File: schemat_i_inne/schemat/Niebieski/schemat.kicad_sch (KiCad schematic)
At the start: 30 parts, among them J1 Hole1, J2 Hole2, J3 Hole3, J4 Hole4, J5 RJ45, SW1 SW_DIP_x01, SW2 Left, SW3 Up, SW4 Down, SW5 Right, SW6 Jump, SW7 Punch, U1 ATmega32A-AU, U2 L7805, U3 WG12864B-STBL, U4 LF33_TO252, U5 SN74LS07, U6 SD, Y1 16Mhz

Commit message: Good footprints, before changes on PCB
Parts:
- U5: footprint Package_TO_SOT_SMD:TO-252-2 -> Package_DIP:DIP-14_W7.62mm_LongPads
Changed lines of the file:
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@@
     (property "Reference" "U5" (id 0) (at 166.37 54.7202 0))
     (property "Value" "SN74LS07" (id 1) (at 166.37 57.2571 0))
-    (property "Footprint" "Package_TO_SOT_SMD:TO-252-2" (id 2) (at 166.37 62.23 0)
+    (property "Footprint" "Package_DIP:DIP-14_W7.62mm_LongPads" (id 2) (at 166.37 62.23 0)
       (effects (font (size 1.27 1.27)) hide)
     )
@@
       (effects (font (size 1.27 1.27)) (justify left))
     )
-    (property "Footprint" "Package_TO_SOT_SMD:TO-252-2" (id 2) (at 226.06 30.48 0)
+    (property "Footprint" "Package_DIP:DIP-14_W7.62mm_LongPads" (id 2) (at 226.06 30.48 0)
       (effects (font (size 1.27 1.27)) hide)
     )
@@
     (property "Reference" "U5" (id 0) (at 165.1 67.4202 0))
     (property "Value" "SN74LS07" (id 1) (at 165.1 69.9571 0))
-    (property "Footprint" "Package_TO_SOT_SMD:TO-252-2" (id 2) (at 165.1 74.93 0)
+    (property "Footprint" "Package_DIP:DIP-14_W7.62mm_LongPads" (id 2) (at 165.1 74.93 0)
       (effects (font (size 1.27 1.27)) hide)
     )
@@
     (property "Reference" "U5" (id 0) (at 165.1 29.3202 0))
     (property "Value" "SN74LS07" (id 1) (at 165.1 31.8571 0))
-    (property "Footprint" "Package_TO_SOT_SMD:TO-252-2" (id 2) (at 165.1 36.83 0)
+    (property "Footprint" "Package_DIP:DIP-14_W7.62mm_LongPads" (id 2) (at 165.1 36.83 0)
       (effects (font (size 1.27 1.27)) hide)
     )
@@
     (property "Reference" "U5" (id 0) (at 165.1 42.0202 0))
     (property "Value" "SN74LS07" (id 1) (at 165.1 44.5571 0))
-    (property "Footprint" "Package_TO_SOT_SMD:TO-252-2" (id 2) (at 165.1 49.53 0)
+    (property "Footprint" "Package_DIP:DIP-14_W7.62mm_LongPads" (id 2) (at 165.1 49.53 0)
       (effects (font (size 1.27 1.27)) hide)
     )
@@
     )
     (path "/6cfeab45-cb3f-4496-a149-1dcab4f48b9e"
-      (reference "U5") (unit 1) (value "SN74LS07") (footprint "Package_TO_SOT_SMD:TO-252-2")
+      (reference "U5") (unit 1) (value "SN74LS07") (footprint "Package_DIP:DIP-14_W7.62mm_LongPads")
     )
     (path "/97028cc7-c78a-4d63-bf12-fed98ab2a824"
-      (reference "U5") (unit 2) (value "SN74LS07") (footprint "Package_TO_SOT_SMD:TO-252-2")
+      (reference "U5") (unit 2) (value "SN74LS07") (footprint "Package_DIP:DIP-14_W7.62mm_LongPads")
     )
     (path "/143f8ad6-39a7-42cd-8611-e300b4175f5e"
-      (reference "U5") (unit 3) (value "SN74LS07") (footprint "Package_TO_SOT_SMD:TO-252-2")
+      (reference "U5") (unit 3) (value "SN74LS07") (footprint "Package_DIP:DIP-14_W7.62mm_LongPads")
     )
     (path "/5c70e1c2-d58b-40cb-968e-ca7279c6263b"
-      (reference "U5") (unit 4) (value "SN74LS07") (footprint "Package_TO_SOT_SMD:TO-252-2")
+      (reference "U5") (unit 4) (value "SN74LS07") (footprint "Package_DIP:DIP-14_W7.62mm_LongPads")
     )
     (path "/2e4c2d57-8d82-46dc-a18a-d07a5b5f91e8"
-      (reference "U5") (unit 7) (value "SN74LS07") (footprint "Package_TO_SOT_SMD:TO-252-2")
+      (reference "U5") (unit 7) (value "SN74LS07") (footprint "Package_DIP:DIP-14_W7.62mm_LongPads")
     )
     (path "/cd6fa7d4-14f3-428e-b040-5de477b5d49d"

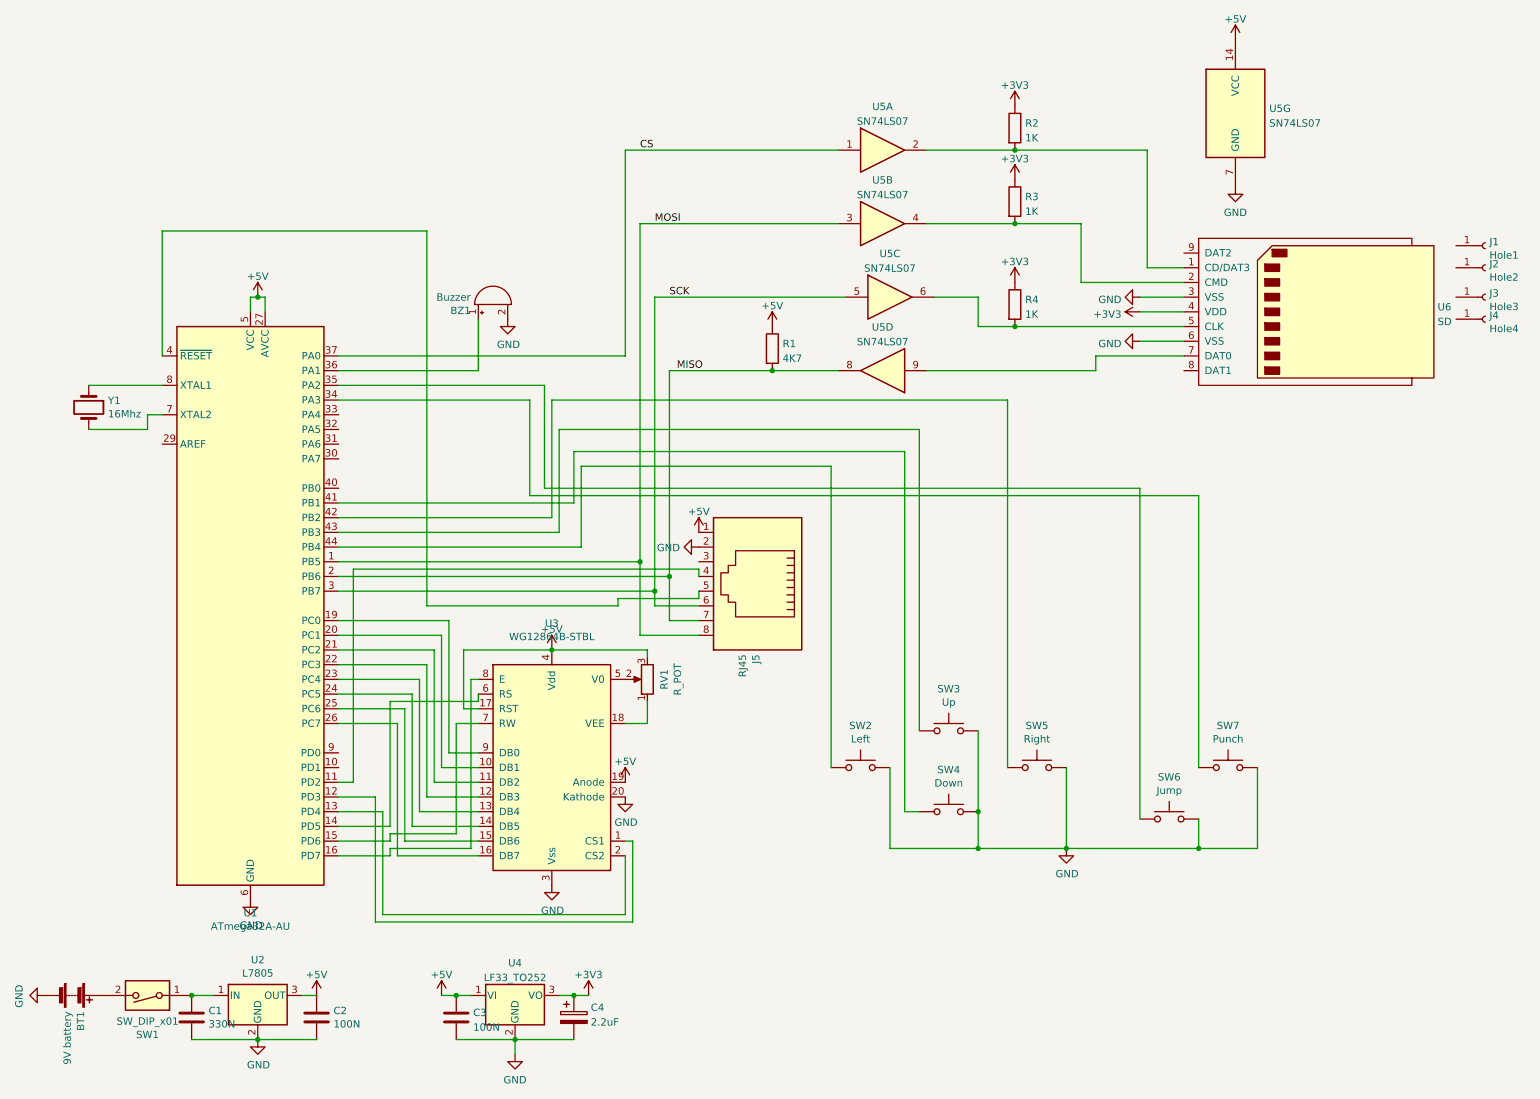
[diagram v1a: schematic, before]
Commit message: Wstepne sciezki z buforem
-> Dodano wstepne sciezki razem z buforem
-> Tam gdzie bylo to wymagane zmieniono warstwe
-> Dodano oporniki 0R we wlasciwych miejscach
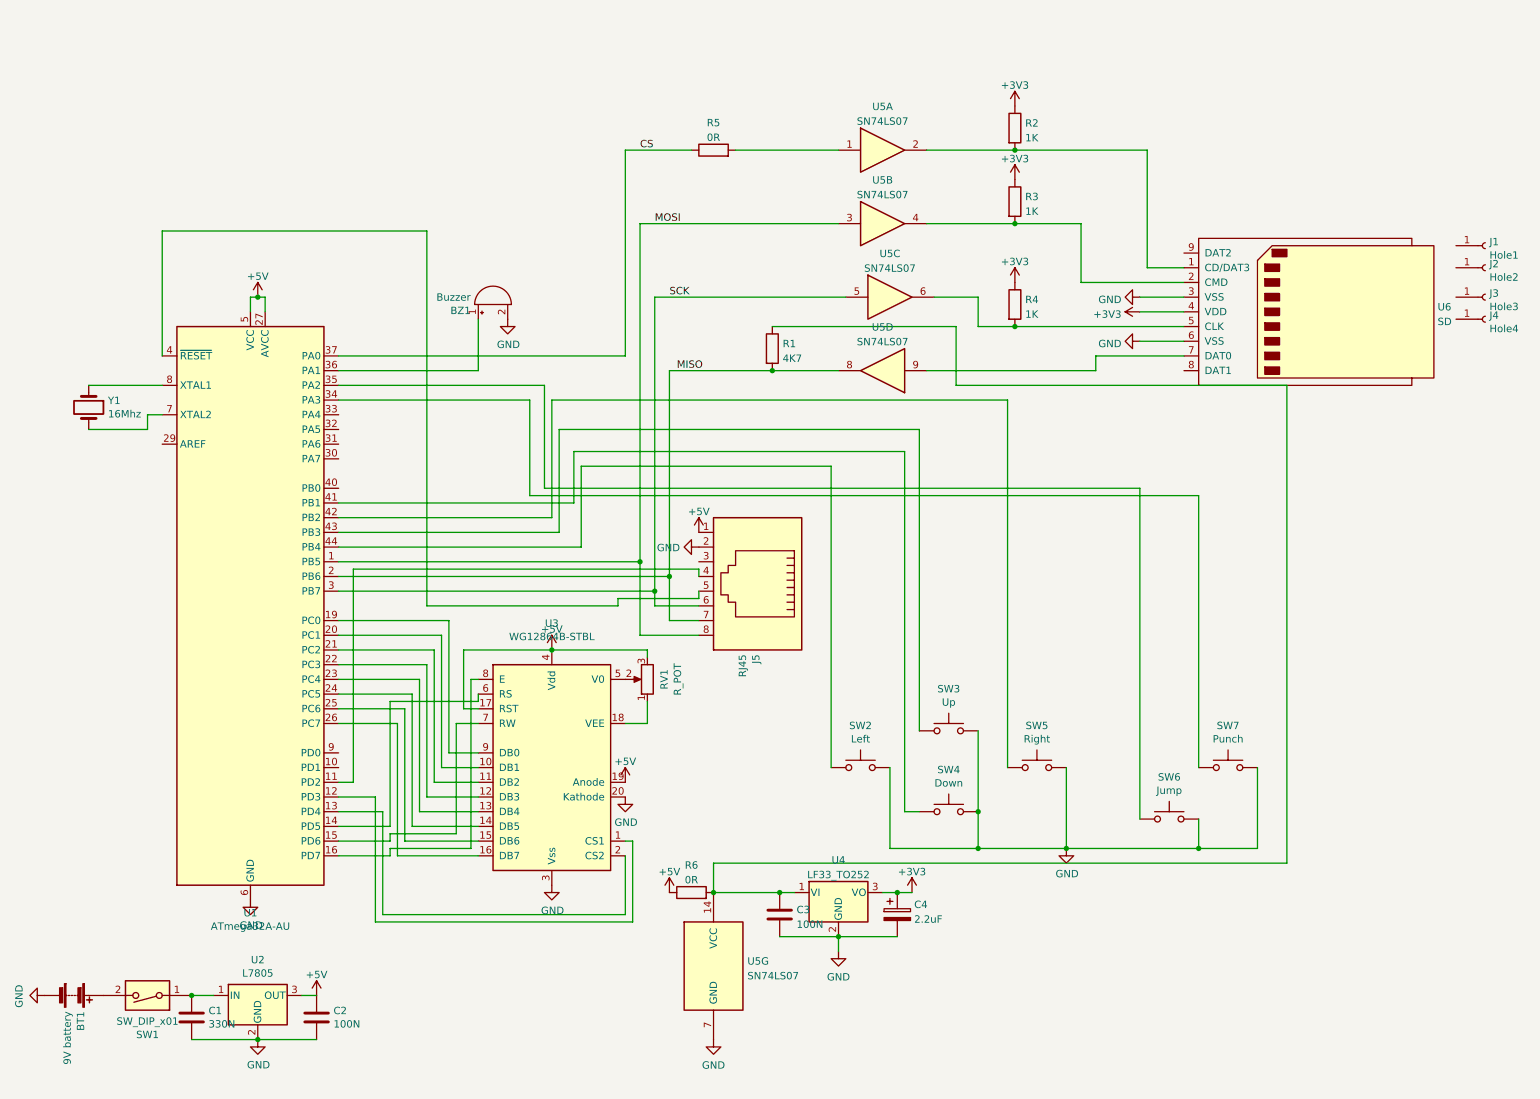
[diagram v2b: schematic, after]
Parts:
- added R5, R6: 0R, Resistor_THT:R_Axial_DIN0207_L6.3mm_D2.5mm_P10.16mm_Horizontal, symbol Device:R
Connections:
- net +5V: now also R6.1; no longer C3.1, R1.1, U4.1 (VI), U5.14 (VCC)
- net CS: now also R5.1; no longer U5.1
- new net: C3.1, R1.1, R6.2, U4.1 (VI), U5.14 (VCC)
- new net: R5.2, U5.1
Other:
- moved on the sheet: C3, C4, U4, U5G

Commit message: Awful but should work v2
-> Wszystko zostalo prowizorycznie podlaczone
-> uzyto 3 opornikow 0R
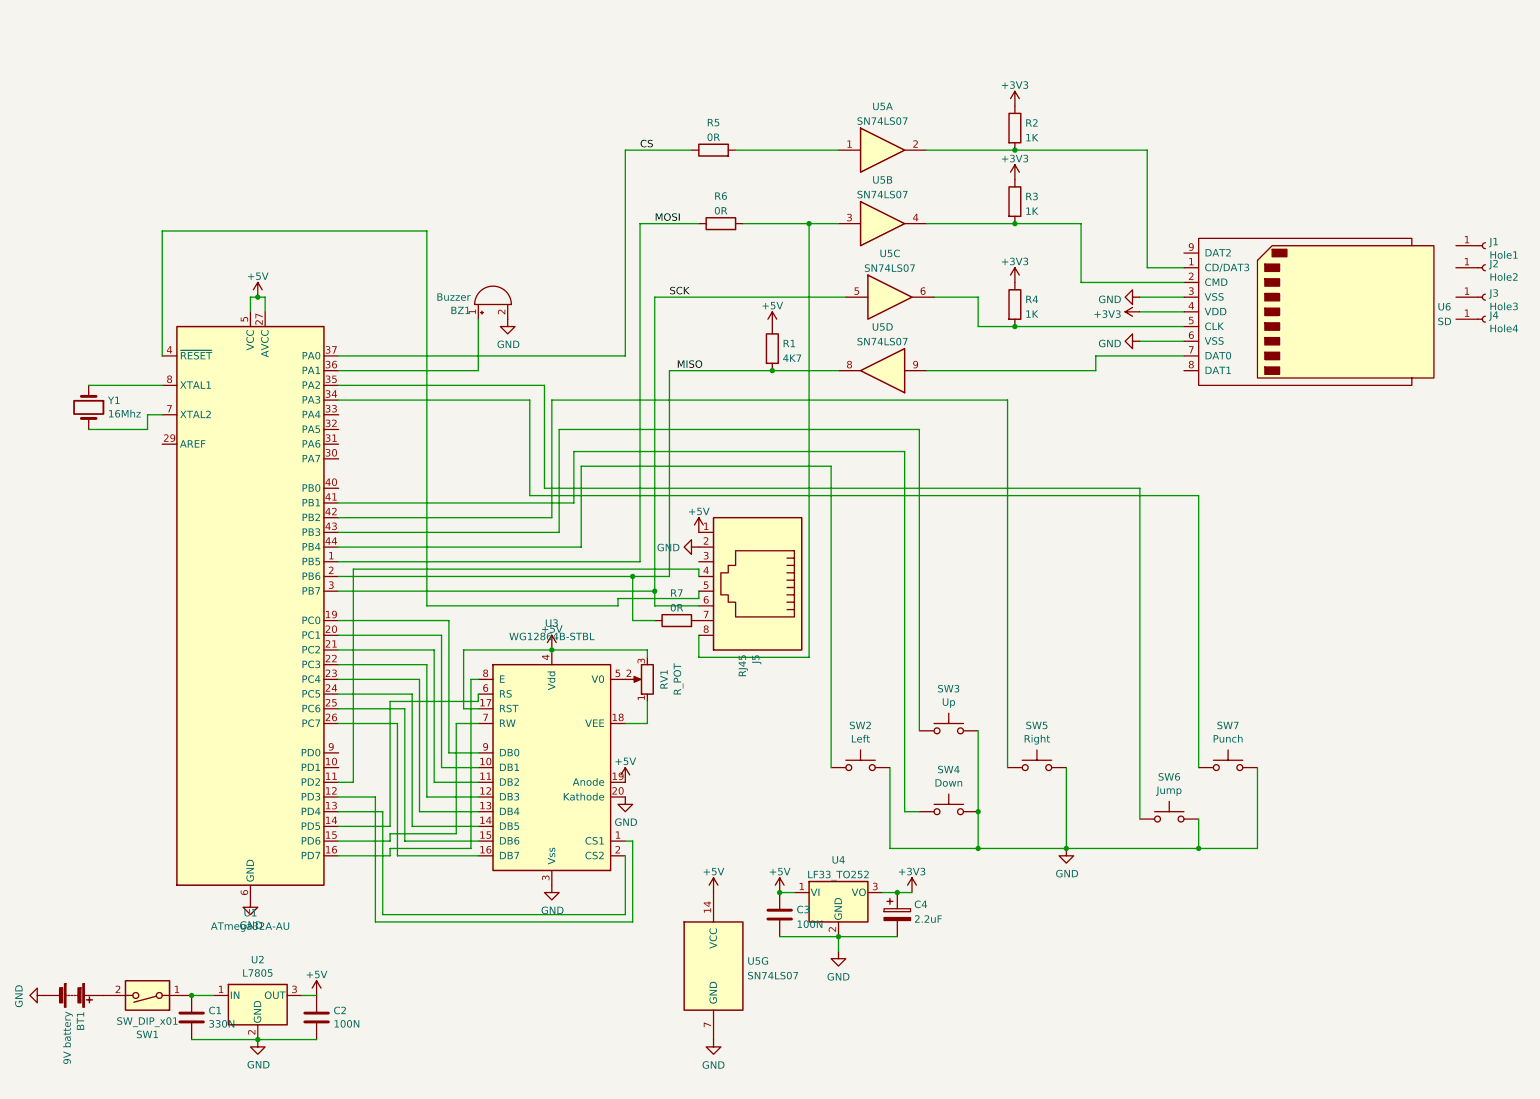
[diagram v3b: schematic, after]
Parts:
- added R7: 0R, Resistor_THT:R_Axial_DIN0204_L3.6mm_D1.6mm_P2.54mm_Vertical, symbol Device:R
- R5: footprint Resistor_THT:R_Axial_DIN0207_L6.3mm_D2.5mm_P10.16mm_Horizontal -> Resistor_THT:R_Axial_DIN0207_L6.3mm_D2.5mm_P15.24mm_Horizontal
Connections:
- net +5V: now also C3.1, R1.1, U4.1 (VI), U5.14 (VCC); no longer R6.1
- net MISO: now also R7.1; no longer J5.7
- net MOSI: now also R6.1; no longer J5.8, U5.3
- new net: J5.7, R7.2
- new net: J5.8, R6.2, U5.3

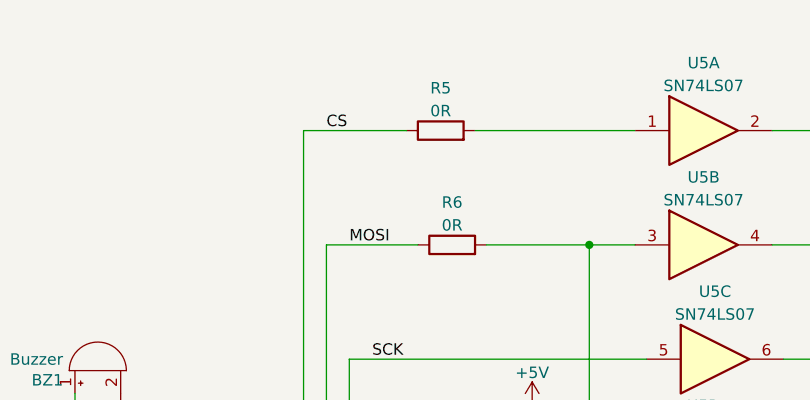
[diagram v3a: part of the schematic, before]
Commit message: Ukonczone polaczenia
-> skonczone polaczenia poprawionego schematu
po przeniesieniu karty
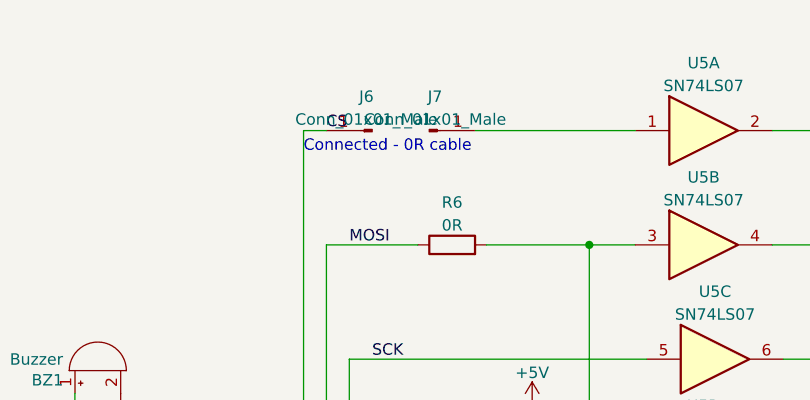
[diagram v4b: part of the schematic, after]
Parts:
- removed R5: 0R, Resistor_THT:R_Axial_DIN0207_L6.3mm_D2.5mm_P15.24mm_Horizontal, symbol Device:R
- added J6, J7: Conn_01x01_Male, Connector_PinHeader_2.54mm:PinHeader_1x01_P2.54mm_Vertical, symbol Connector:Conn_01x01_Male
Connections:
- net CS: now also J6.1 (Pin_1)
- net at U5.1: now also J7.1 (Pin_1)
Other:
- note added: "Connected - 0R cable"
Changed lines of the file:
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@@
-    (stroke (width 0) (type default) (color 0 0 0 0))
-  )
-  (wire (pts (xy 120.65 36.83) (xy 132.08 36.83))
     (stroke (width 0) (type default) (color 0 0 0 0))
   )
@@
     (stroke (width 0) (type default) (color 0 0 0 0))
   )
+  (wire (pts (xy 120.65 36.83) (xy 123.19 36.83))
+    (stroke (width 0) (type default) (color 0 0 0 0))
+  )
   (wire (pts (xy 92.71 123.19) (xy 107.95 123.19))
     (stroke (width 0) (type default) (color 0 0 0 0))
@@
   (wire (pts (xy 123.19 49.53) (xy 123.19 107.95))
     (stroke (width 0) (type default) (color 0 0 0 0))
+  )
+  (text "Connected - 0R cable\n" (at 120.65 39.37 0)
+    (effects (font (size 1.27 1.27)) (justify left bottom))
   )
   (label "CS" (at 123.19 36.83 0)
@@
     (pin "1")
   )
+  (symbol (lib_id "Connector:Conn_01x01_Male") (at 128.27 36.83 180) (unit 1)
+    (in_bom yes) (on_board yes)
+    (property "Reference" "J6" (id 0) (at 127.635 33.054 0))
+    (property "Value" "Conn_01x01_Male" (id 1) (at 127.635 35.5909 0))
+    (property "Footprint" "Connector_PinHeader_2.54mm:PinHeader_1x01_P2.54mm_Vertical" (id 2) (at 128.27 36.83 0)
+      (effects (font (size 1.27 1.27)) hide)
+    )
+    (property "Datasheet" "~" (id 3) (at 128.27 36.83 0)
+      (effects (font (size 1.27 1.27)) hide)
+    )
+    (pin "1")
+  )
   (symbol (lib_id "power:+3V3") (at 187.96 59.69 0) (unit 1)
     (in_bom yes) (on_board yes) (fields_autoplaced)
@@
     (pin "1")
     (pin "2")
+  )
+  (symbol (lib_id "Connector:Conn_01x01_Male") (at 134.62 36.83 0) (unit 1)
+    (in_bom yes) (on_board yes) (fields_autoplaced)
+    (property "Reference" "J7" (id 0) (at 135.255 33.054 0))
+    (property "Value" "Conn_01x01_Male" (id 1) (at 135.255 35.5909 0))
+    (property "Footprint" "Connector_PinHeader_2.54mm:PinHeader_1x01_P2.54mm_Vertical" (id 2) (at 134.62 36.83 0)
+      (effects (font (size 1.27 1.27)) hide)
+    )
+    (property "Datasheet" "~" (id 3) (at 134.62 36.83 0)
+      (effects (font (size 1.27 1.27)) hide)
+    )
+    (pin "1")
   )
   (symbol (lib_id "power:+3V3") (at 187.96 29.21 0) (unit 1)
@@
     (pin "1")
   )
-  (symbol (lib_id "Device:R") (at 135.89 36.83 90) (unit 1)
-    (in_bom yes) (on_board yes) (fields_autoplaced)
-    (property "Reference" "R5" (id 0) (at 135.89 32.1142 90))
-    (property "Value" "0R" (id 1) (at 135.89 34.6511 90))
-    (property "Footprint" "Resistor_THT:R_Axial_DIN0207_L6.3mm_D2.5mm_P15.24mm_Horizontal" (id 2) (at 135.89 38.608 90)
-      (effects (font (size 1.27 1.27)) hide)
-    )
-    (property "Datasheet" "~" (id 3) (at 135.89 36.83 0)
-      (effects (font (size 1.27 1.27)) hide)
-    )
-    (pin "1")
-    (pin "2")
-  )
   (symbol (lib_id "power:+3V3") (at 170.18 165.1 0) (unit 1)
     (in_bom yes) (on_board yes) (fields_autoplaced)
@@
       (reference "J5") (unit 1) (value "RJ45") (footprint "Connector_RJ:RJ45_Amphenol_54602-x08_Horizontal")
     )
+    (path "/48c77641-1046-44b0-bae8-52da953ea633"
+      (reference "J6") (unit 1) (value "Conn_01x01_Male") (footprint "Connector_PinHeader_2.54mm:PinHeader_1x01_P2.54mm_Vertical")
+    )
+    (path "/766ddc19-af5a-4e09-a63d-aa90e0de5dee"
+      (reference "J7") (unit 1) (value "Conn_01x01_Male") (footprint "Connector_PinHeader_2.54mm:PinHeader_1x01_P2.54mm_Vertical")
+    )
     (path "/99f25f45-592b-4240-9f1f-264696d255dd"
       (reference "R1") (unit 1) (value "4K7") (footprint "Resistor_SMD:R_0805_2012Metric_Pad1.20x1.40mm_HandSolder")
@@
       (reference "R4") (unit 1) (value "1K") (footprint "Resistor_SMD:R_0805_2012Metric_Pad1.20x1.40mm_HandSolder")
     )
-    (path "/ec5eb3ca-2664-450c-8b1d-e0936f9ba60f"
-      (reference "R5") (unit 1) (value "0R") (footprint "Resistor_THT:R_Axial_DIN0207_L6.3mm_D2.5mm_P15.24mm_Horizontal")
-    )
     (path "/703624fe-b513-41fe-8f55-1fe8de97703d"
